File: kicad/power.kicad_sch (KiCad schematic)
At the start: 64 parts, among them J1 USB_C_Receptacle_USB2.0_16P, J2 Pack NTC, J3 XT30 pack, Q1 AO4407A, SW1 Power, U4 AP64500SP-13, U5 CH224A, U7 BQ25798, U8 HT7550-1, U9 AP2112K-3.3

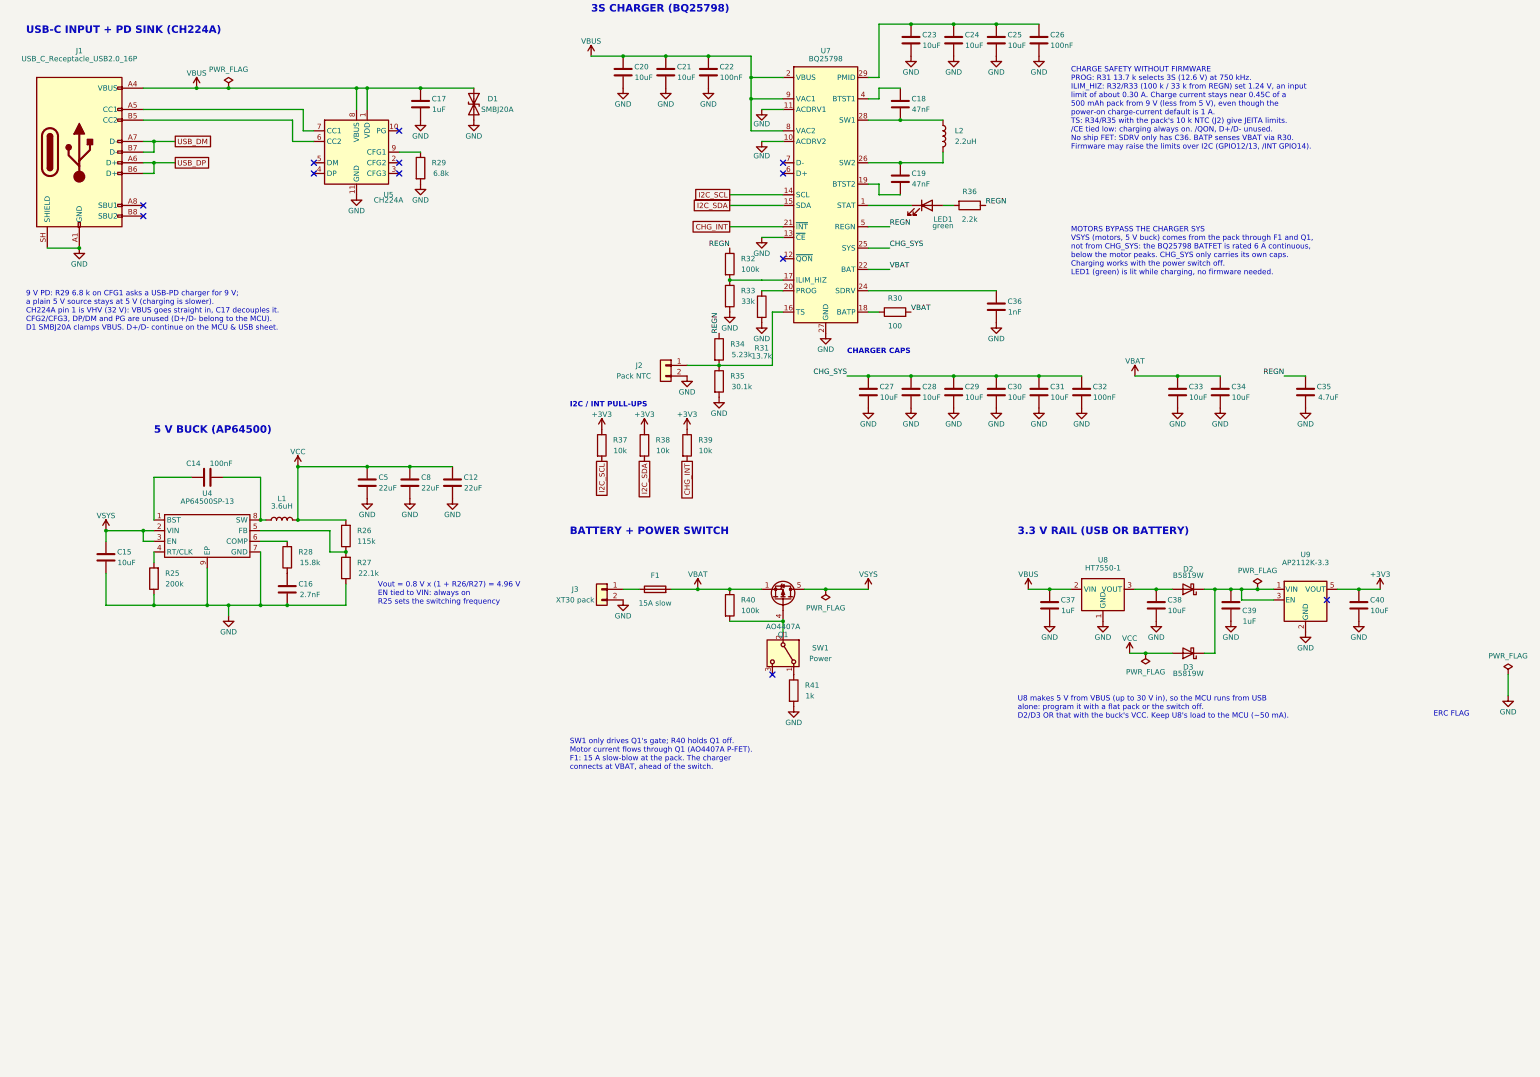
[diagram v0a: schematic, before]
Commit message: Lay out rev 2 with an internal pack, protector and cost-down parts
Board is 91 x 47 mm for a 96 x 52 mm enclosure, with placement and hand
power routing done; signal routing is still to do.

- Internal Gens Ace 3S 1000 mAh pack on an XT60 pigtail, protected on the
  board by a BQ7791501 with back-to-back low-side FETs and a 2.5 mOhm
  shunt, plus a balance header and two NTCs.
- USB-A and USB-C on the top edge, IO as a recessed 3 x 6 pin block, GPIO
  map re-swapped for the placement, USB nets renamed with P/N suffixes
  for the diff-pair router.
- Cost-down swaps that keep every feature: basic or preferred passives
  and ICs, cheaper connectors, a THT power switch rated for 12.6 V, and
  replacements for the low-stock TH1 and Q2/Q3. L3 is Digi-Key sourced
  and hand-placed.
- Net classes and design rules, rev 2 power-net widths in review.py, and
  the PCB critic and loop updated for rev 2.

Schematic review passes; PCB review passes every gate except unrouted.

Co-Authored-By: Claude Opus 5.5 <noreply@anthropic.com>
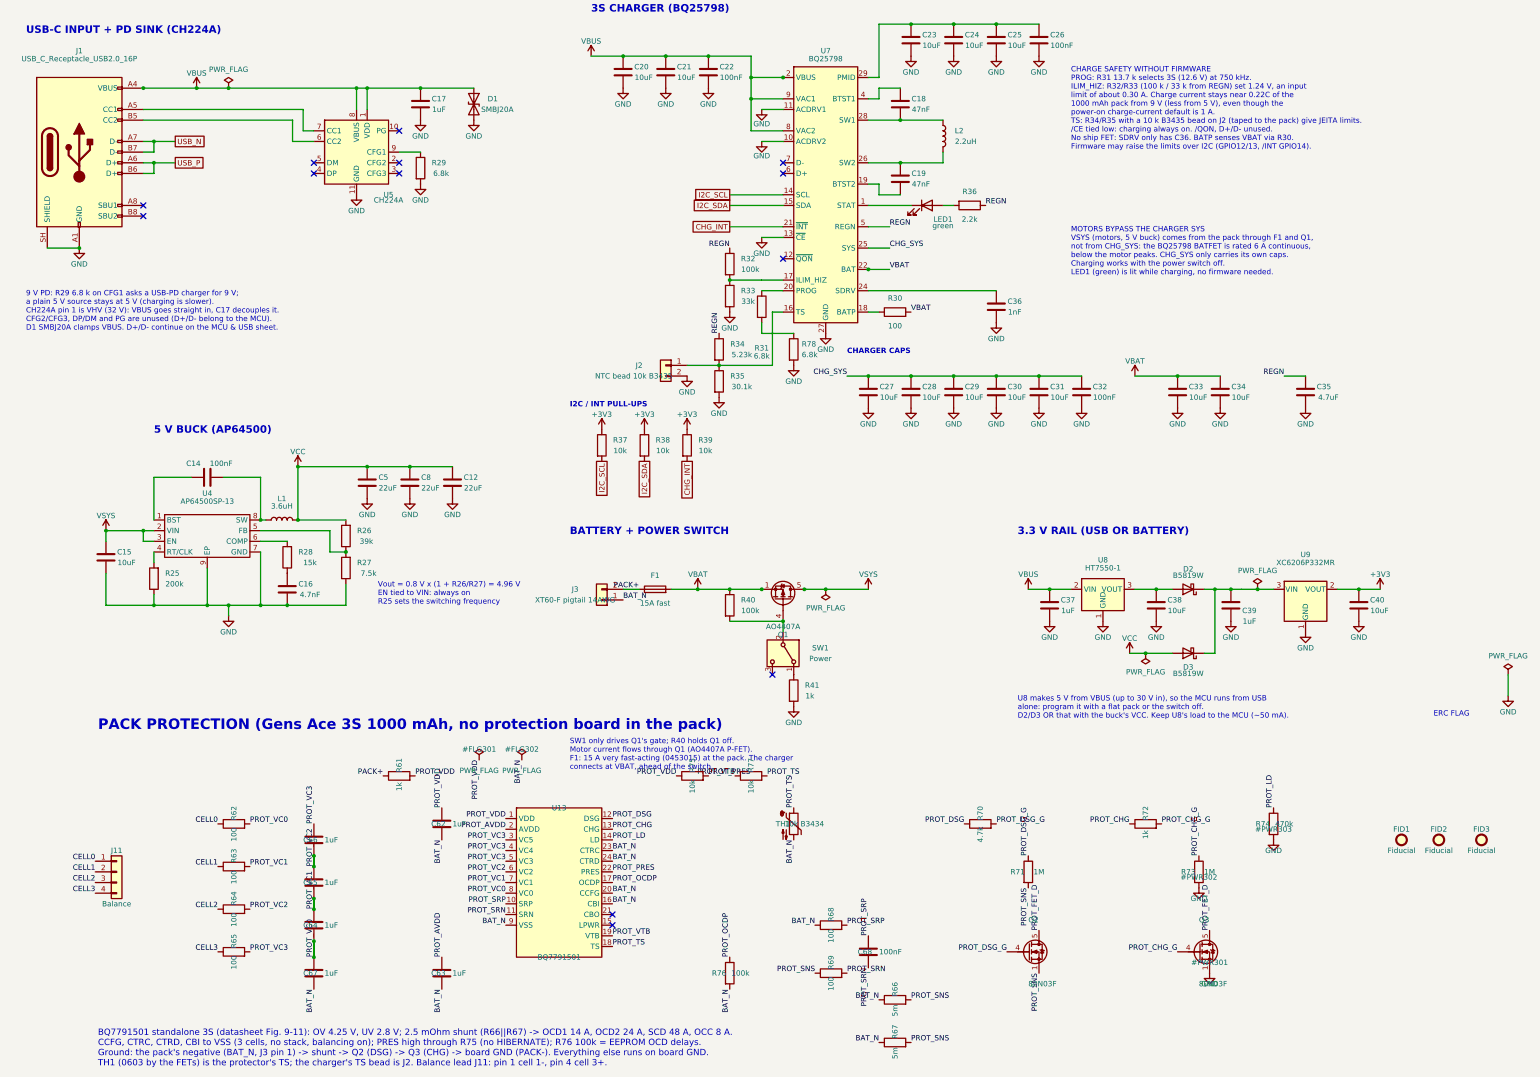
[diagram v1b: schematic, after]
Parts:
- added C62, C63, C64, C65, C66, C67: 1uF, Capacitor_SMD:C_0402_1005Metric, symbol Device:C
- added C68: 100nF, Capacitor_SMD:C_0402_1005Metric, symbol Device:C
- added FID1, FID2, FID3: Fiducial, Fiducial:Fiducial_1mm_Mask2mm, symbol Mechanical:Fiducial
- added J11: Balance, Connector_JST:JST_XH_B4B-XH-A_1x04_P2.50mm_Vertical, symbol Connector_Generic:Conn_01x04
- added Q2, Q3: 80N03F, Package_TO_SOT_SMD:TDSON-8-1, symbol Transistor_FET:BSC026N08NS5
- added R61, R72: 1k, Resistor_SMD:R_0402_1005Metric, symbol Device:R
- added R62, R63, R64, R65, R68, R69: 100, Resistor_SMD:R_0402_1005Metric, symbol Device:R
- added R66, R67: 5m, Resistor_SMD:R_2512_6332Metric, symbol Device:R
- added R70: 4.7k, Resistor_SMD:R_0402_1005Metric, symbol Device:R
- added R71, R73: 1M, Resistor_SMD:R_0402_1005Metric, symbol Device:R
- added R74: 470k, Resistor_SMD:R_0402_1005Metric, symbol Device:R
- added R75, R77: 10k, Resistor_SMD:R_0402_1005Metric, symbol Device:R
- added R76: 100k, Resistor_SMD:R_0402_1005Metric, symbol Device:R
- added R78: 6.8k, Resistor_SMD:R_0402_1005Metric, symbol Device:R
- added TH1: 10k B3434, Resistor_SMD:R_0603_1608Metric, symbol Device:Thermistor_NTC
- added U13: BQ7791501, Package_SO:TSSOP-24_4.4x7.8mm_P0.65mm, symbol hexyhustle:BQ77915
- C12, C5, C8: footprint Capacitor_SMD:C_0805_2012Metric -> Capacitor_SMD:C_1206_3216Metric; LCSC Part # C45783 -> C5672; MPN CL21A226MAQNNNE -> CL31A226KPHNNNE
- C16: value 2.7nF -> 4.7nF; LCSC Part # C45185 -> C1538; MPN 0402B272K500NT -> 0402B472K500NT
- C17, C37: LCSC Part # C5673 -> C15849; MPN CL10A105KA8NNNC -> CL10A105KB8NNNC
- C18, C19: footprint Capacitor_SMD:C_0402_1005Metric -> Capacitor_SMD:C_0603_1608Metric; LCSC Part # C318631 -> C1622; MPN CL05B473KA5NNNC -> 0603B473K500NT; Manufacturer Samsung Electro-Mechanics -> FH (Guangdong Fenghua)
- D1: LCSC Part # C364296 -> C19077575; Manufacturer MDD -> hongjiacheng
- F1: value 15A slow -> 15A fast
- J1: footprint Connector_USB:USB_C_Receptacle_HRO_TYPE-C-31-M-12 -> hexy:USB_C_Receptacle_ShouHan_TYPE-C16PIN; LCSC Part # C165948 -> C393939; MPN TYPE-C-31-M-12 -> TYPE-C16PIN; Manufacturer Korean Hroparts Elec -> SHOU HAN
- J2: value Pack NTC -> NTC bead 10k B3435; footprint Connector_JST:JST_PH_S2B-PH-K_1x02_P2.00mm_Horizontal -> Connector_Wire:SolderWire-0.1sqmm_1x02_P3.6mm_D0.4mm_OD1mm; LCSC Part # C173752 -> (none); MPN S2B-PH-K-S(LF)(SN) -> (none); Manufacturer JST -> (none)
- J3: value XT30 pack -> XT60-F pigtail 14AWG; footprint Connector_AMASS:AMASS_XT30PW-M_1x02_P2.50mm_Horizontal -> Connector_Wire:SolderWire-2sqmm_1x02_P7.8mm_D2mm_OD3.9mm; LCSC Part # C431092 -> (none); MPN XT30PW-M -> (none); Manufacturer Changzhou Amass -> (none)
- L2: footprint Inductor_SMD:L_Sunlord_MWSA0402S -> Inductor_SMD:L_Changjiang_FNR4030S; LCSC Part # C408335 -> C167869; MPN MWSA0402S-2R2MT -> FNR4030S2R2MT; Manufacturer Sunlord -> Changjiang Microelectronics
- LED1: footprint LED_SMD:LED_0603_1608Metric -> LED_SMD:LED_0805_2012Metric; LCSC Part # C12624 -> C2297; MPN KT-0603G -> KT-0805G
- R26: value 115k -> 39k; LCSC Part # C25747 -> C25783; MPN 0402WGF1153TCE -> 0402WGF3902TCE
- R27: value 22.1k -> 7.5k; LCSC Part # C43473 -> C25918; MPN 0402WGF2212TCE -> 0402WGF7501TCE
- R28: value 15.8k -> 15k; LCSC Part # C26956 -> C25756; MPN 0402WGF1582TCE -> 0402WGF1502TCE
- R31: value 13.7k -> 6.8k; LCSC Part # C25854 -> C25917; MPN 0402WGF1372TCE -> 0402WGF6801TCE
- SW1: footprint Button_Switch_SMD:SW_SPDT_Shouhan_MSK12C02 -> hexy:SW_SPDT_ShouHan_SK12D07VG4; LCSC Part # C431540 -> C393937; MPN MSK12C02 -> SK12D07VG4
- U9: value AP2112K-3.3 -> XC6206P332MR; footprint Package_TO_SOT_SMD:SOT-23-5 -> Package_TO_SOT_SMD:SOT-23-3; symbol Regulator_Linear:AP2112K-3.3 -> hexyhustle:XC6206P332MR; LCSC Part # C51118 -> C5446; MPN AP2112K-3.3TRG1 -> XC6206P332MR-G; Manufacturer Diodes Incorporated -> Torex Semicon
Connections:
- net +3V3: now also U9.2 (VOUT); no longer U9.5 (VOUT)
- net GND: now also U9.1 (GND), Q3.1 (S), Q3.2 (S), Q3.3 (S), R73.2, R74.2, R78.2; no longer J3.2 (Pin_2), R31.2, U9.2 (GND)
- net BAT_N: now reaches J3.1 (Pin_1)
- net BAT_N: now also C62.2, C63.2, C67.2, R66.1, R67.1, R68.1, R76.2, TH1.2, U13.16 (CBI), U13.20 (CCFG), U13.23 (CTRC), U13.24 (CTRD), U13.9 (VSS); no longer F1.1
- net at C39.1, D2.1 (K), D3.1 (K)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: no longer U9.1 (VIN)
- net USB_DM renamed USB_N
- net USB_DP renamed USB_P
- new net: R31.2, R78.1
- new net CELL0: J11.1 (Pin_1), R62.1
- new net CELL1: J11.2 (Pin_2), R63.1
- new net CELL2: J11.3 (Pin_3), R64.1
- new net CELL3: J11.4 (Pin_4), R65.1
- new net PACK+: F1.1, J3.2 (Pin_2), R61.1
- new net PROT_AVDD: C63.1, U13.2 (AVDD)
- new net PROT_CHG: R72.1, U13.13 (CHG)
- new net PROT_CHG_G: Q3.4 (G), R72.2, R73.1
- new net PROT_DSG: R70.1, U13.12 (DSG)
- new net PROT_DSG_G: Q2.4 (G), R70.2, R71.1
- new net PROT_FET_D: Q2.5 (D), Q3.5 (D)
- new net PROT_LD: R74.1, U13.14 (LD)
- new net PROT_OCDP: R76.1, U13.17 (OCDP)
- new net PROT_PRES: R75.2, U13.22 (PRES)
- new net PROT_SNS: Q2.1 (S), Q2.2 (S), Q2.3 (S), R66.2, R67.2, R69.1, R71.2
- new net PROT_SRN: C68.2, R69.2, U13.11 (SRN)
- new net PROT_SRP: C68.1, R68.2, U13.10 (SRP)
- new net PROT_TS: R77.2, TH1.1, U13.18 (TS)
- new net PROT_VC0: C64.2, C67.1, R62.2, U13.8 (VC0)
- new net PROT_VC1: C64.1, C65.2, R63.2, U13.7 (VC1)
- new net PROT_VC2: C65.1, C66.2, R64.2, U13.6 (VC2)
- new net PROT_VC3: C66.1, R65.2, U13.3 (VC5), U13.4 (VC4), U13.5 (VC3)
- new net PROT_VDD: C62.1, R61.2, R75.1, U13.1 (VDD)
- new net PROT_VTB: R77.1, U13.19 (VTB)
- no-connect marks 12 -> 13
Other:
- note added: "BQ7791501 standalone 3S (datasheet Fig. 9-11): OV 4.25 V, UV 2.8 V; 2.5 mOhm shunt (R66||R67) -> OCD1 14 A, OCD2 24 A, SCD 48 A, OCC 8 A. CCFG, CTRC, CTRD, CBI to VSS (3 cells, no stack, balancing on); PRES high through R75 (no HIBERNATE); R76 100k = EEPROM OCD delays. Ground: the pack's negative (BAT_N, J3 pin 1) -> shunt -> Q2 (DSG) -> Q3 (CHG) -> board GND (PACK-). Everything else runs on boar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"
- note added: "CHARGE SAFETY WITHOUT FIRMWARE PROG: R31 13.7 k selects 3S (12.6 V) at 750 kHz. ILIM_HIZ: R32/R33 (100 k / 33 k from REGN) set 1.24 V, an input limit of about 0.30 A. Charge current stays near 0.22C of the 1000 mAh pack from 9 V (less from 5 V), even though the power-on charge-current default is 1 A. TS: R34/R35 with a 10 k B3435 bead on J2 (taped to the pack) give JEITA limits. /CE tied low: cha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"
- note added: "PACK PROTECTION (Gens Ace 3S 1000 mAh, no protection board in the pack)"
- note added: "SW1 only drives Q1's gate; R40 holds Q1 off. Motor current flows through Q1 (AO4407A P-FET). F1: 15 A very fast-acting (0453015) at the pack. The charger connects at VBAT, ahead of the switch."
- note removed: "CHARGE SAFETY WITHOUT FIRMWARE PROG: R31 13.7 k selects 3S (12.6 V) at 750 kHz. ILIM_HIZ: R32/R33 (100 k / 33 k from REGN) set 1.24 V, an input limit of about 0.30 A. Charge current stays near 0.45C of a 500 mAh pack from 9 V (less from 5 V), even though the power-on charge-current default is 1 A. TS: R34/R35 with the pack's 10 k NTC (J2) give JEITA limits. /CE tied low: charging always on. /QON,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"
- note removed: "SW1 only drives Q1's gate; R40 holds Q1 off. Motor current flows through Q1 (AO4407A P-FET). F1: 15 A slow-blow at the pack. The charger connects at VBAT, ahead of the switch."
- moved on the sheet: J3
